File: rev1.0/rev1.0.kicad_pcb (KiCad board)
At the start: 4 copper layers, 40.6 x 15.9 mm, 18 parts, among them J1 Conn_01x06_Pin, J3 Conn_01x06_Socket, J4 Conn_01x06_Socket, U1 74HC595, U2 74HC595, U3 74HC165

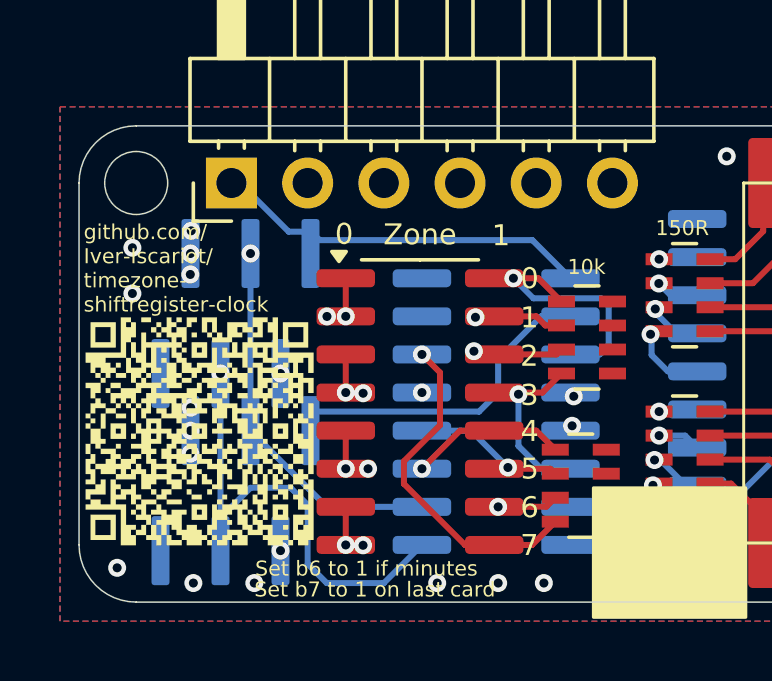
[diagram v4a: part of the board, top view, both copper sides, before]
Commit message: Started coding.
Reading and writing to registers implemented.
The circuit is now on rev 1.1, but there were some mistakes on this one to, hehe.
The dip-switch is NOT the same size as a 16p soic, a little wider (bodgedd by bending pins under on one side (the one thats just all vcc anyways, as it can be bridged if you're struggeling with the jank solder)).
The socket also has some mechanical solder points on the ends, that wasnt on my footprint. They are also thinner and longer than thought. The mechanical solder on one side could short some pins on the 165, but i simply put a piece of kapton tape acrross the pins. Circuit works otherwise. Perhaps a little hot. Maybe not ideal to drive LEDs directly from 595's, but they can probably handle it
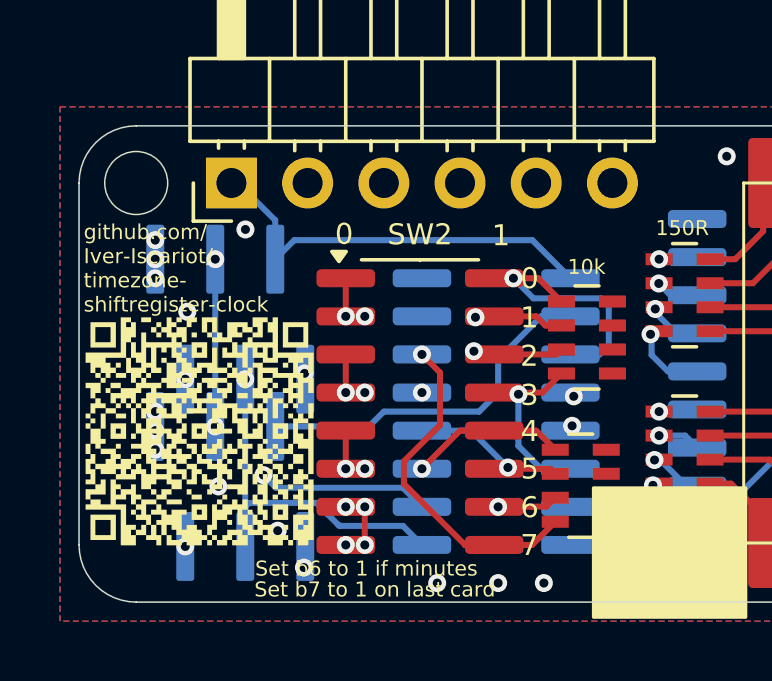
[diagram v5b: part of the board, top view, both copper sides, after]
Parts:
- moved J4 0.26 mm to (207.0, 100.4)
- moved J3 0.22 mm to (207.0, 106.0)
- renumbered Zone to SW2
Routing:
- net Shift/load: track 55.1 -> 51.5 mm
- net Clock: track 46.5 -> 48.7 mm, vias 3 -> 5
- net PISO in: track 10.8 -> 12.0 mm
- net SIPO in: track 31.4 -> 30.3 mm
- net SIPO out: track 23.5 -> 22.6 mm
- net PISO out: track 13.4 -> 13.9 mm
- net VCC: track 21.0 -> 21.5 mm, vias 29 -> 31
- net GND: vias 16 -> 17
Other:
- board text added: "TimeZone clock REV 1.1"
- board text removed: "TimeZone clock REV 1.0"
